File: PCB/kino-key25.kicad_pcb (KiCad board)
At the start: 2 copper layers, 215 x 83 mm, 129 parts, among them J1 AudioJack3, J2 AudioJack3, Q1 BSS138, SW1 SW_SPST, SW10 SW_SPST, SW11 SW_SPST, SW12 SW_SPST, SW13 SW_SPST, SW14 SW_SPST, SW15 SW_SPST, SW16 SW_SPST, SW17 SW_SPST, SW18 SW_SPST, SW19 SW_SPST, SW2 SW_SPST, SW20 SW_SPST, SW21 SW_SPST, SW22 SW_SPST, SW23 SW_SPST, SW24 SW_SPST, SW25 SW_SPST, SW26 SW_SPST, SW27 SW_SPST, SW28 SW_SPST, SW29 SW_SPST, SW3 SW_SPST, SW30 SW_SPST, SW31 SW_SPST, SW4 SW_SPST, SW5 SW_SPST, SW6 SW_SPST, SW7 SW_SPST, SW8 SW_SPST, SW9 SW_SPST, U1 74HC165, U2 74HC165, U3 MOUDLE-SEEEDUINO-XIAO, U4 74HC165, U5 74HC165, U6 BAS40DW-04-7-F, U7 TLP2361_TPL_E, U8 CD74HC4050PWR/74HC4050PW

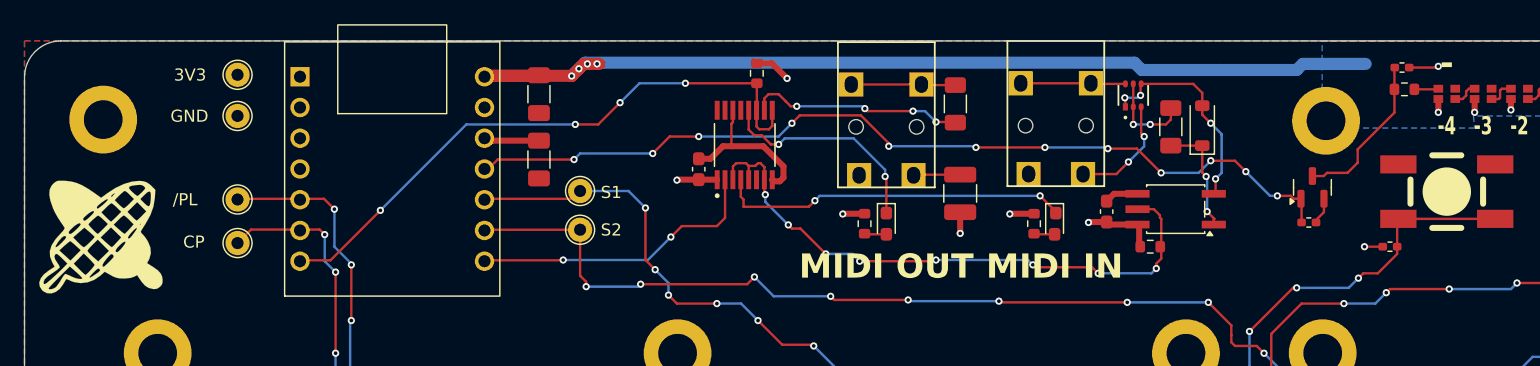
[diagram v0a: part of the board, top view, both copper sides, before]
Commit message: [PCB] Update to KiCad 9.0, remove voltage conversion #6
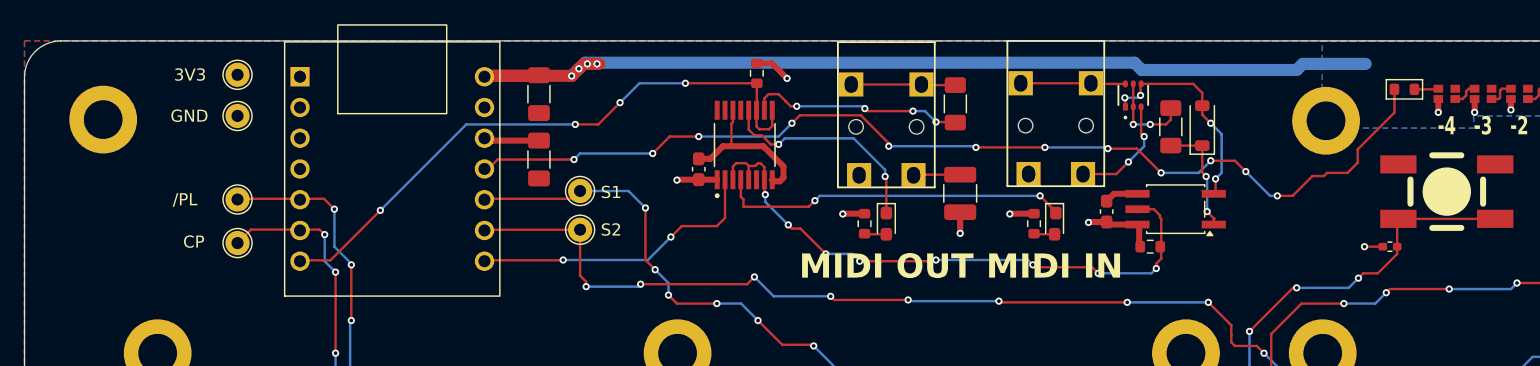
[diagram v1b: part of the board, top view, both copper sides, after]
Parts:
- removed G***: LOGO, my_footprint:kinoshita-logo_simplified_300dpi
- removed Q1: BSS138, Package_TO_SOT_SMD:SOT-23
- removed R35, R43: 10k, Resistor_SMD:R_0402_1005Metric_Pad0.72x0.64mm_HandSolder
- R44: footprint Resistor_SMD:R_0603_1608Metric -> PCM_Resistor_SMD_AKL:R_0603_1608Metric
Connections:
- net NEOPIXEL Out 5V renamed Net-(D1-DI)
- R44 pad 1: Net-(Q1-D) -> NEOPIXEL Out
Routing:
- net Net-(Q1-D): track 13.3 -> 0.00 mm
- net NEOPIXEL Out: track 74.7 -> 85.7 mm
- net VBUS: track 97.7 -> 95.2 mm, vias 18 -> 17
- net Net-(Q1-S): track 2.23 -> 0.00 mm
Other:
- board text removed: "-"
